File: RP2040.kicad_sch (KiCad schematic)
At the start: 27 parts, among them J6 USB_B_Micro, J7 Conn_01x02, U2 AMS1117-3.3, U6 W25Q128JVS, U7 RP2040, Y1 X322512MSB4SI

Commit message: RP2040 wired up, warning cleanup
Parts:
- U2: footprint CJ4-Autopilot:SOT-223-4NC -> Package_TO_SOT_SMD:SOT-223-3_TabPin2
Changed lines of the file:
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@@
     (property "Reference" "U2" (id 0) (at 64.77 18.6182 0))
     (property "Value" "AMS1117-3.3" (id 1) (at 64.77 20.9296 0))
-    (property "Footprint" "CJ4-Autopilot:SOT-223-4NC" (id 2) (at 64.77 19.685 0)
+    (property "Footprint" "Package_TO_SOT_SMD:SOT-223-3_TabPin2" (id 2) (at 64.77 19.685 0)
       (effects (font (size 1.27 1.27)) hide)
     )

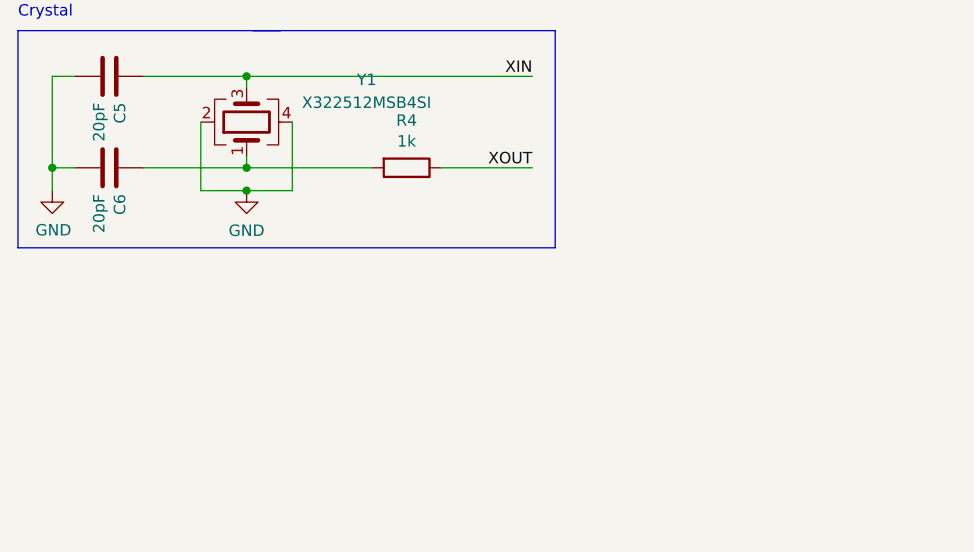
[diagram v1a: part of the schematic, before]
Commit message: Update encoder footprint, USB trace width
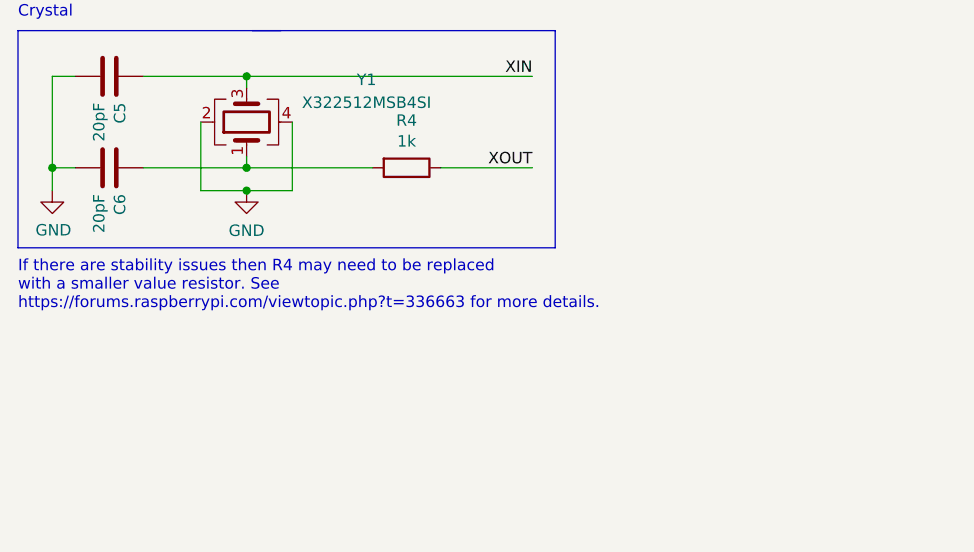
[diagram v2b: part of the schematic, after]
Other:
- note added: "If there are stability issues then R4 may need to be replaced with a smaller value resistor. See https://forums.raspberrypi.com/viewtopic.php?t=336663 for more details."
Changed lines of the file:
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@@
+    (effects (font (size 1.27 1.27)) (justify left bottom))
+  )
+  (text "If there are stability issues then R4 may need to be replaced\nwith a smaller value resistor. See \nhttps://forums.raspberrypi.com/viewtopic.php?t=336663 for more details."
+    (at 13.97 139.7 0)
     (effects (font (size 1.27 1.27)) (justify left bottom))
   )

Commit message: More missing versions
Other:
- title: (none) -> CJ4 Autopilot Panel
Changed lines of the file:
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@@
 (kicad_sch (version 20211123) (generator eeschema)
   (paper "A4")
+  (title_block
+    (title "CJ4 Autopilot Panel")
+    (date "2022-08-30")
+    (rev "@version@")
+    (comment 1 "neile@live.com")
+    (comment 2 "Neil Enns")
+  )
   (junction (at 179.07 41.91) (diameter 0) (color 0 0 0 0)
   )

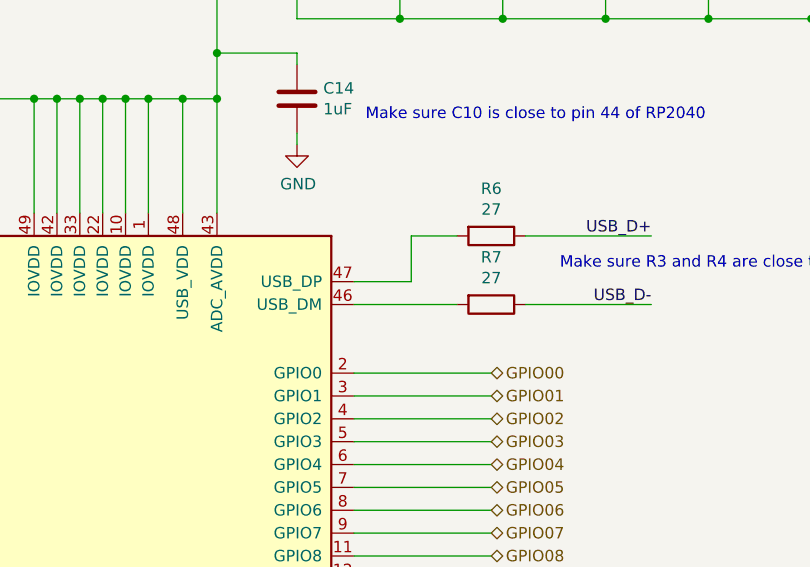
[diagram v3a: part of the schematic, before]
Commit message: Add missing net labels
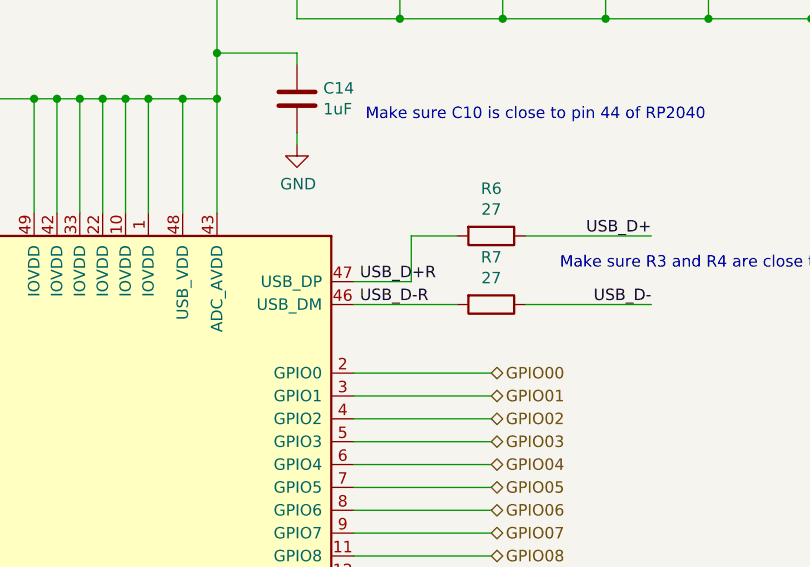
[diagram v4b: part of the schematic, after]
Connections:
- net USB_D-R: now reaches R7.2, U7.46 (USB_DM)
- net USB_D+R: now reaches R6.2, U7.47 (USB_DP)
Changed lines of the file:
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@@
+    (effects (font (size 1.27 1.27)) (justify left bottom))
+  )
+  (label "USB_D-R" (at 212.725 64.77 0)
     (effects (font (size 1.27 1.27)) (justify left bottom))
   )
@@
     (effects (font (size 1.27 1.27)) (justify left bottom))
   )
+  (label "USB_D+R" (at 212.725 62.23 0)
+    (effects (font (size 1.27 1.27)) (justify left bottom))
+  )

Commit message: Update crystal capacitors
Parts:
- C5, C6: value 20pF -> 10pF; LCSC C1554 -> C32949
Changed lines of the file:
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@@
       (effects (font (size 1.27 1.27)) (justify left))
     )
-    (property "Value" "20pF" (id 1) (at 22.987 126.746 0)
+    (property "Value" "10pF" (id 1) (at 22.987 126.746 0)
       (effects (font (size 1.27 1.27)) (justify left))
     )
@@
       (effects (font (size 1.27 1.27)) hide)
     )
-    (property "LCSC" "C1554" (id 5) (at 24.13 123.825 0)
+    (property "LCSC" "C32949" (id 5) (at 24.13 123.825 0)
       (effects (font (size 1.27 1.27)) hide)
     )
@@
       (effects (font (size 1.27 1.27)) (justify left))
     )
-    (property "Value" "20pF" (id 1) (at 22.987 116.586 0)
+    (property "Value" "10pF" (id 1) (at 22.987 116.586 0)
       (effects (font (size 1.27 1.27)) (justify left))
     )
@@
       (effects (font (size 1.27 1.27)) hide)
     )
-    (property "LCSC" "C1554" (id 5) (at 24.13 113.665 0)
-      (effects (font (size 1.27 1.27)) hide)
-    )
+    (property "LCSC" "C32949" (id 5) (at 24.13 113.665 0)
+      (effects (font (size 1.27 1.27)) hide)
+    )
